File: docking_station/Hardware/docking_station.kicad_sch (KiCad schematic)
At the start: 56 parts, among them IC1 VOM1271T, IC2 VOM1271T, IC3 VOM1271T, IC4 VOM1271T, IC5 VOM1271T, J1 SUPPLY_EN, J2 LIVE_IN, J5 SUPPLY+, J6 SUPPLY-, K1 RELPOL R40N-3021-85-1024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

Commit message: almost done
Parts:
- added Q12: 2N7002K, Package_TO_SOT_SMD:SOT-23, symbol Transistor_FET:2N7002K
- R3: value 1k5 -> 170
- R6, R9: value 50k -> 10k
- R8: value 200k -> 500k
- RV1, RV2: value R_Potentiometer -> 20k
- U2, U6: value Comparator -> MCP6561T-E/OT
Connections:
- net +5V: now also R3.2, R6.2; no longer R6.1
- net CH_END: now also U6.4, Q12.1 (G); no longer R3.2
- net GND: now also Q12.2 (S); no longer IC5.2 (K_1)
- net at C7.1, R8.1, U6.3 (+): now also R7.1; no longer R7.2
- net at U2.4: now also R7.2; no longer R7.1
- net at RV1.1: now also R6.1; no longer R6.2
- new net: IC5.2 (K_1), Q12.3 (D)
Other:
- note added: "DELAY CIRCUIT"
- note added: "HISTEREZA"
- note added: "LOW CURRENT FLAG"
- note removed: "COMPARATOR"
- note removed: "WYBRAĆ OPAMPA I KOMPARATOR"
- moved on the sheet: C4, C5, C7, C8, IC5, J1, J2, K1, Q10, Q11, R3, R8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

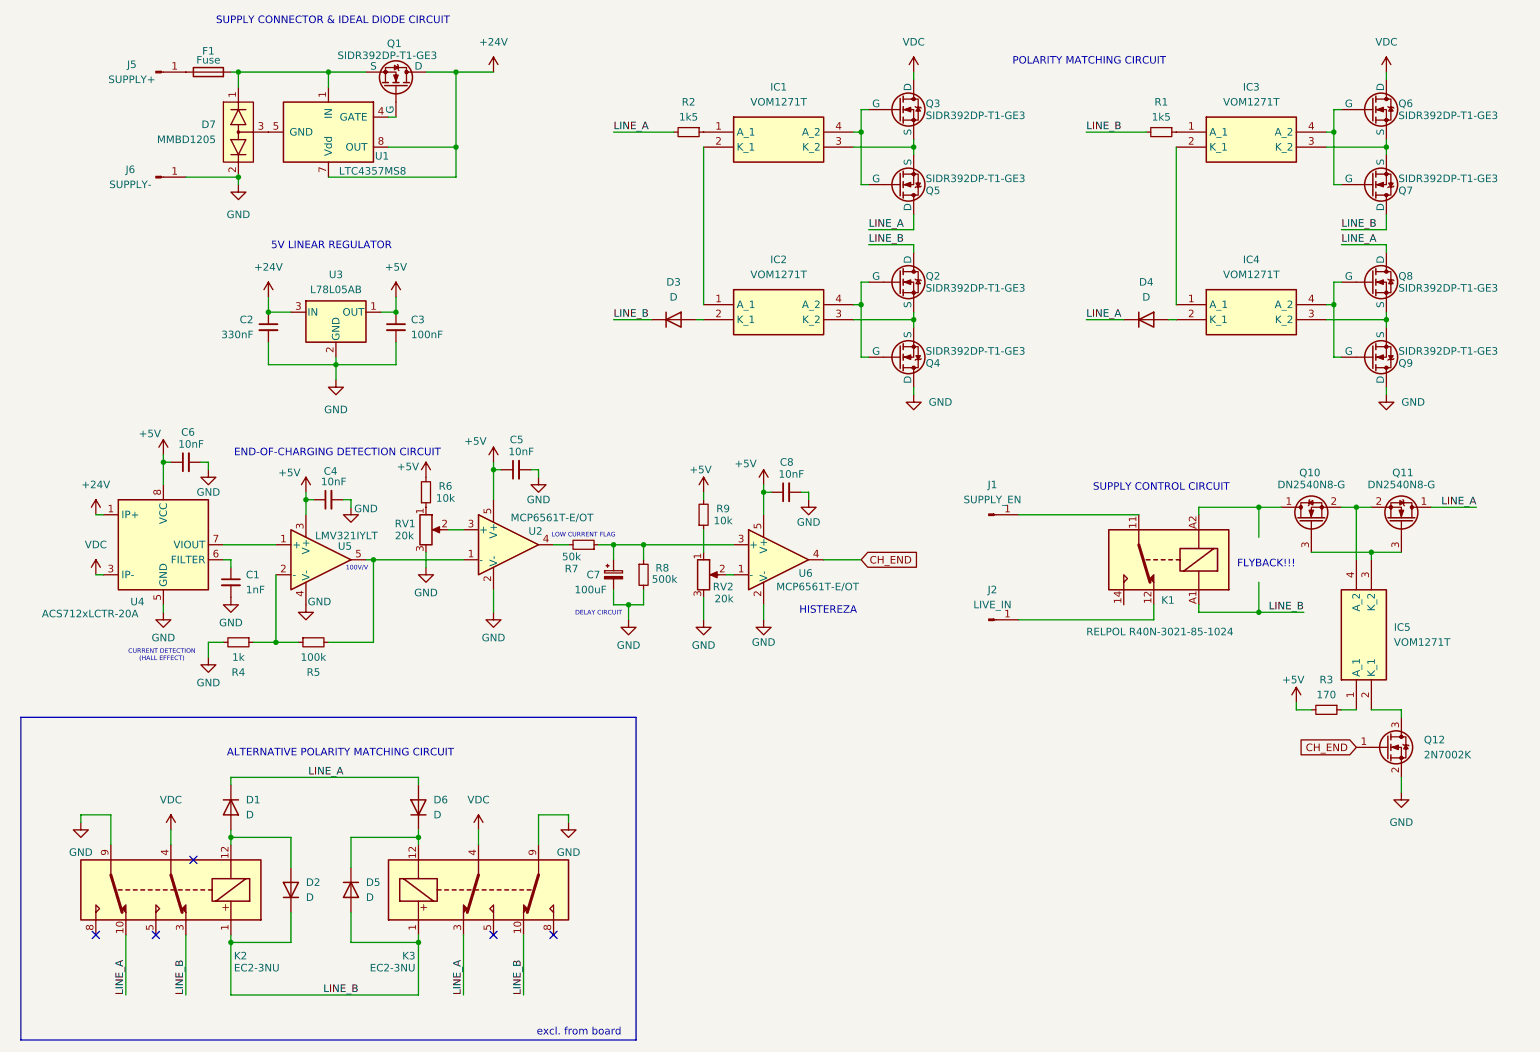
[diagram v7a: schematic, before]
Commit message: finished (v1, no flyback yet)
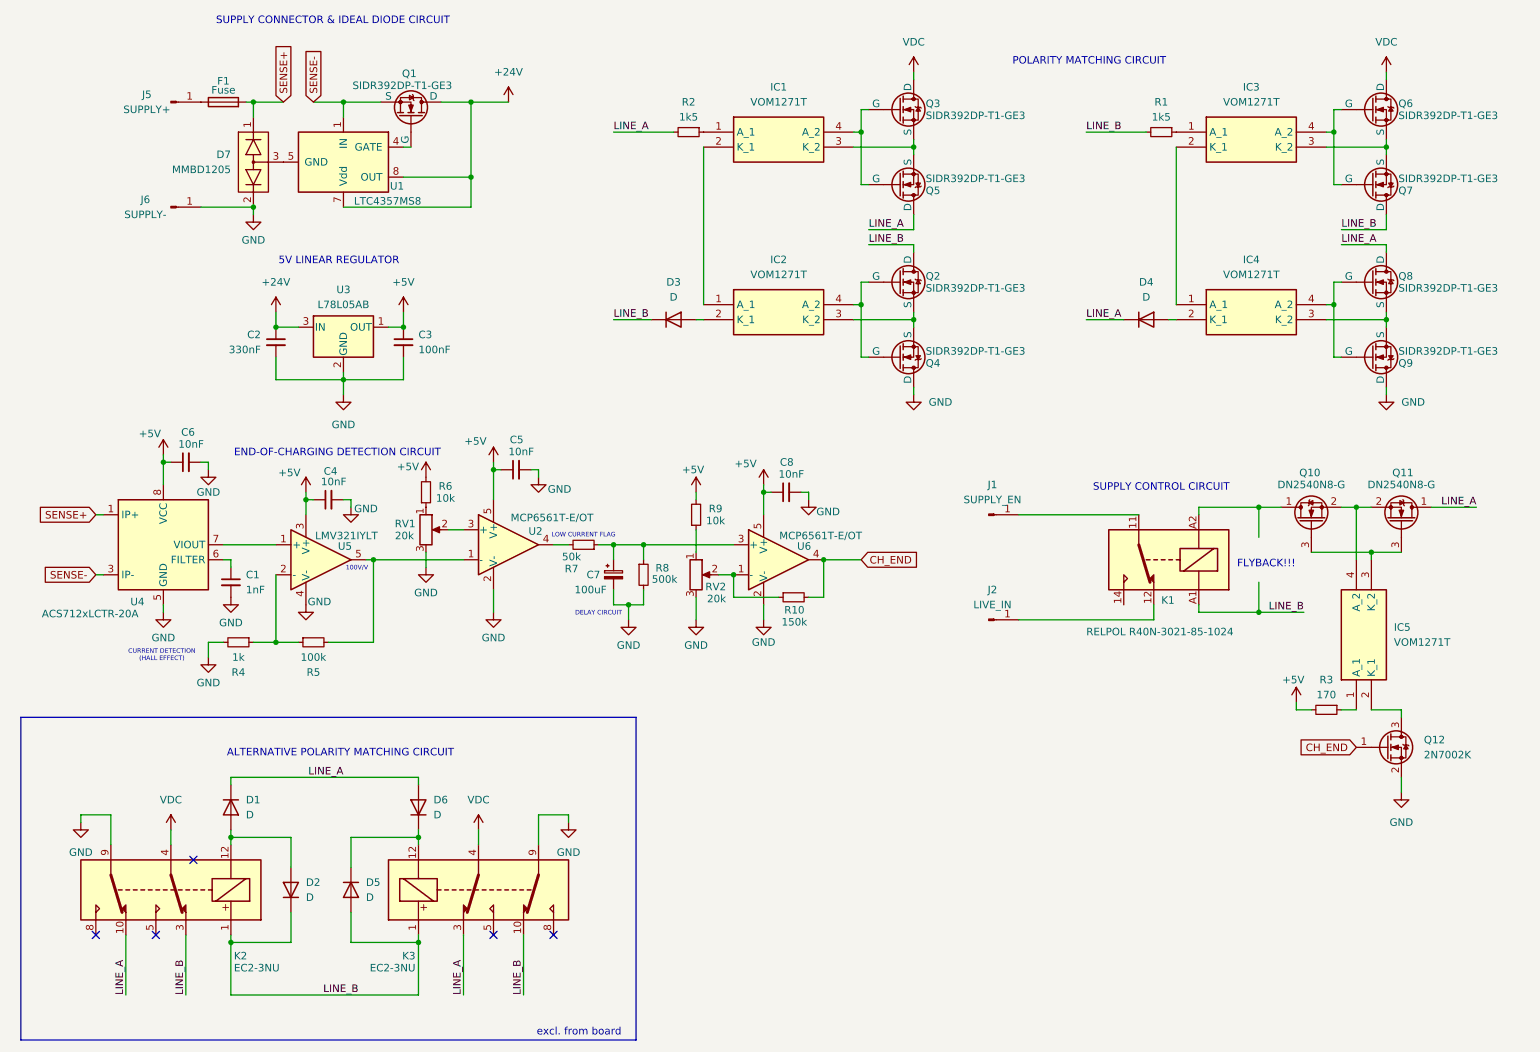
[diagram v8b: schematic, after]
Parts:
- added R10: 150k, symbol Device:R_Small
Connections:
- net +24V: no longer U4.1 (IP+), U4.2 (IP+)
- net CH_END: now also R10.2
- net VDC: no longer U4.3 (IP-), U4.4 (IP-)
- net SENSE+: now reaches D7.1, F1.2
- net SENSE+: now also U4.1 (IP+), U4.2 (IP+); no longer Q1.1 (S), U1.1 (IN)
- net at RV2.2, U6.1 (-): now also R10.1
- new net SENSE-: Q1.1 (S), U1.1 (IN), U4.3 (IP-), U4.4 (IP-)
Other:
- note removed: "HISTEREZA"
- moved on the sheet: C2, C3, D7, F1, J5, J6, Q1, R9, RV2, U1, U3
